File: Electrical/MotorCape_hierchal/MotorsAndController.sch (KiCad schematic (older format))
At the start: 5 parts, among them J1 Motor1, J2 DualMotorController_PWR, J4 DualMotorController_SIG, J5 Motor2

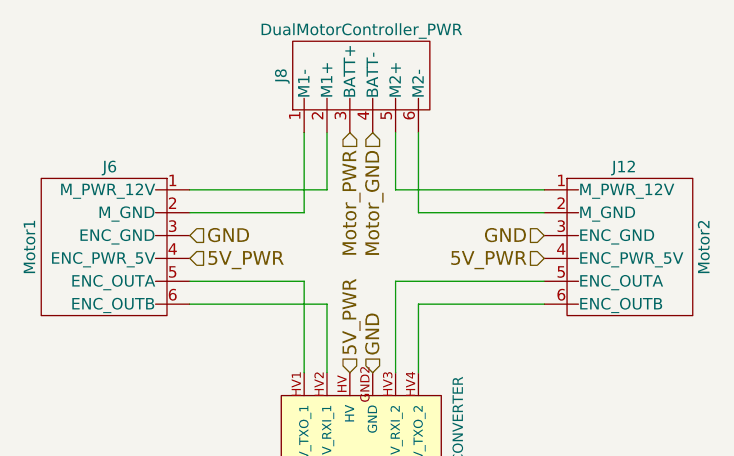
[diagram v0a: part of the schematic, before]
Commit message: trying to lay-out things. lots of via's, this could be a bit messy
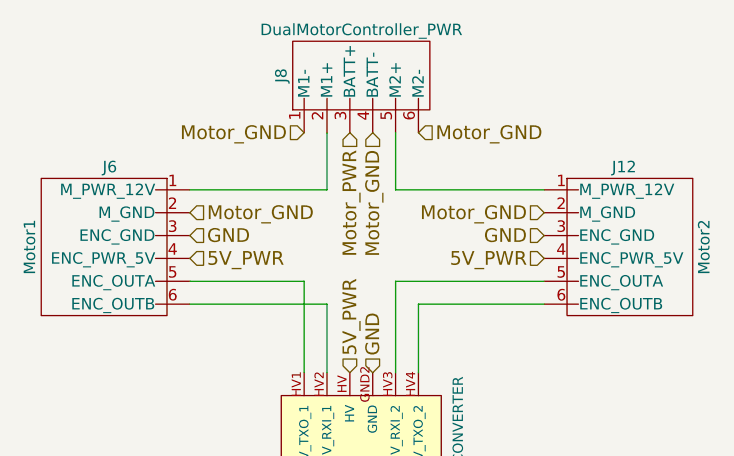
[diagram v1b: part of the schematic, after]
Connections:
- net Motor_GND: now also J1.2 (M_GND), J2.1 (M1-), J2.6 (M2-), J5.2 (M_GND)
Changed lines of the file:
@@
 $Descr A4 11693 8268
 encoding utf-8
-Sheet 3 4
+Sheet 2 4
 Title ""
 Date ""
@@
 $EndComp
 Wire Wire Line
-	3300 1700 3300 1950
-Wire Wire Line
-	3300 1950 2700 1950
-Wire Wire Line
-	3200 1700 3200 2050
-Wire Wire Line
-	3200 2050 2700 2050
-Wire Wire Line
-	3700 1700 3700 2050
-Wire Wire Line
-	3700 2050 4250 2050
-Wire Wire Line
 	3600 1700 3600 1950
 Wire Wire Line
@@
 	0    -1   -1   0
 $EndComp
+Wire Wire Line
+	3300 1700 3300 1950
+Wire Wire Line
+	3300 1950 2700 1950
+Text HLabel 2700 2050 2    60   Input ~ 0
+Motor_GND
+Text HLabel 3200 1700 0    60   Input ~ 0
+Motor_GND
+Text HLabel 3700 1700 2    60   Input ~ 0
+Motor_GND
+Text HLabel 4250 2050 0    60   Input ~ 0
+Motor_GND
 $EndSCHEMATC

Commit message: pushing changes while routing. still not done yet
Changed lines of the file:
@@
 AR Path="/5ACB9F03/5AC8852E" Ref="J10"  Part="1"
 AR Path="/5ACC6682/5AC8852E" Ref="J16"  Part="1"
-F 0 "J10" H 3500 5700 50  0000 C CNN
+F 0 "J4" H 3500 5700 50  0000 C CNN
 F 1 "DualMotorController_SIG" V 3300 5400 50  0000 C CNN
 F 2 "MotorCapeComponents:Pin_Header_Latched_1x05" H 3150 5350 50  0001 C CNN
@@
 AR Path="/5ACB9F03/5AC89C0C" Ref="J8"  Part="1"
 AR Path="/5ACC6682/5AC89C0C" Ref="J14"  Part="1"
-F 0 "J8" H 3450 1800 50  0000 C CNN
+F 0 "J2" H 3450 1800 50  0000 C CNN
 F 1 "DualMotorController_PWR" V 3650 1450 50  0000 C CNN
 F 2 "Connectors_Phoenix:PhoenixContact_MSTBA-G_06x5.08mm_Angled" H 3350 1450 50  0001 C CNN
@@
 AR Path="/5ACB9F03/5AC89F1B" Ref="J6"  Part="1"
 AR Path="/5ACC6682/5AC89F1B" Ref="J13"  Part="1"
-F 0 "J6" H 2350 2550 50  0000 C CNN
+F 0 "J1" H 2350 2550 50  0000 C CNN
 F 1 "Motor1" V 2700 2200 50  0000 C CNN
 F 2 "MotorCapeComponents:Pin_Header_Latched_1x06" H 2150 2200 50  0001 C CNN
@@
 AR Path="/5ACB9F03/5AC89F69" Ref="J12"  Part="1"
 AR Path="/5ACC6682/5AC89F69" Ref="J17"  Part="1"
-F 0 "J12" H 4600 2550 50  0000 C CNN
+F 0 "J5" H 4600 2550 50  0000 C CNN
 F 1 "Motor2" V 4950 2200 50  0000 C CNN
 F 2 "MotorCapeComponents:Pin_Header_Latched_1x06" H 4400 2200 50  0001 C CNN
@@
 AR Path="/5ACC6682/5AC8C87A" Ref="B3"  Part="1"
 AR Path="/5ACB9F03/5AC8C87A" Ref="B2"  Part="1"
-F 0 "B2" H 2950 3850 45  0000 L BNN
+F 0 "B1" H 2950 3850 45  0000 L BNN
 F 1 "SPARKFUN_LOGIC_LEVEL_CONVERTER" H 2950 3000 45  0000 L BNN
 F 2 "Sparkfun_Boards:SPARKFUN_LOGIC_LEVEL_CONVERTER" H 3500 3850 20  0001 C CNN

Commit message: pushing latest motor controller layout changes
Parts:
- renumbered J5 to BL1, J1 to FL1, J2 to Left_PWR1, J4 to Left_SIG1, B1 to Left_Shifters1
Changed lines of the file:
@@
 $Descr A4 11693 8268
 encoding utf-8
-Sheet 2 4
+Sheet 3 4
 Title ""
 Date ""
@@
 $EndDescr
 $Comp
-L DualMotorController_Signal J4
+L DualMotorController_Signal Left_SIG1
 U 1 1 5AC8852E
 P 3500 5350
-AR Path="/5AC8802A/5AC8852E" Ref="J4"  Part="1"
+AR Path="/5AC8802A/5AC8852E" Ref="Left_SIG1"  Part="1"
 AR Path="/5ACA5F87/5AC8852E" Ref="J?"  Part="1"
-AR Path="/5ACB9F03/5AC8852E" Ref="J10"  Part="1"
-AR Path="/5ACC6682/5AC8852E" Ref="J16"  Part="1"
-F 0 "J4" H 3500 5700 50  0000 C CNN
+AR Path="/5ACB9F03/5AC8852E" Ref="Top_SIG1"  Part="1"
+AR Path="/5ACC6682/5AC8852E" Ref="Right_SIG1"  Part="1"
+F 0 "Right_SIG1" H 3500 5700 50  0000 C CNN
 F 1 "DualMotorController_SIG" V 3300 5400 50  0000 C CNN
 F 2 "MotorCapeComponents:Pin_Header_Latched_1x05" H 3150 5350 50  0001 C CNN
@@
 M2_DIR
 $Comp
-L DualMotorController_Power J2
+L DualMotorController_Power Left_PWR1
 U 1 1 5AC89C0C
 P 3450 1450
-AR Path="/5AC8802A/5AC89C0C" Ref="J2"  Part="1"
+AR Path="/5AC8802A/5AC89C0C" Ref="Left_PWR1"  Part="1"
 AR Path="/5ACA5F87/5AC89C0C" Ref="J?"  Part="1"
-AR Path="/5ACB9F03/5AC89C0C" Ref="J8"  Part="1"
-AR Path="/5ACC6682/5AC89C0C" Ref="J14"  Part="1"
-F 0 "J2" H 3450 1800 50  0000 C CNN
+AR Path="/5ACB9F03/5AC89C0C" Ref="Top_PWR1"  Part="1"
+AR Path="/5ACC6682/5AC89C0C" Ref="Right_PWR1"  Part="1"
+F 0 "Right_PWR1" H 3450 1800 50  0000 C CNN
 F 1 "DualMotorController_PWR" V 3650 1450 50  0000 C CNN
 F 2 "Connectors_Phoenix:PhoenixContact_MSTBA-G_06x5.08mm_Angled" H 3350 1450 50  0001 C CNN
@@
 $EndComp
 $Comp
-L MotorConnector J1
+L MotorConnector FL1
 U 1 1 5AC89F1B
 P 2350 2200
-AR Path="/5AC8802A/5AC89F1B" Ref="J1"  Part="1"
+AR Path="/5AC8802A/5AC89F1B" Ref="FL1"  Part="1"
 AR Path="/5ACA5F87/5AC89F1B" Ref="J?"  Part="1"
-AR Path="/5ACB9F03/5AC89F1B" Ref="J6"  Part="1"
-AR Path="/5ACC6682/5AC89F1B" Ref="J13"  Part="1"
-F 0 "J1" H 2350 2550 50  0000 C CNN
+AR Path="/5ACB9F03/5AC89F1B" Ref="FlagWheel1"  Part="1"
+AR Path="/5ACC6682/5AC89F1B" Ref="FR1"  Part="1"
+F 0 "FR1" H 2350 2550 50  0000 C CNN
 F 1 "Motor1" V 2700 2200 50  0000 C CNN
 F 2 "MotorCapeComponents:Pin_Header_Latched_1x06" H 2150 2200 50  0001 C CNN
@@
 $EndComp
 $Comp
-L MotorConnector J5
+L MotorConnector BL1
 U 1 1 5AC89F69
 P 4600 2200
-AR Path="/5AC8802A/5AC89F69" Ref="J5"  Part="1"
+AR Path="/5AC8802A/5AC89F69" Ref="BL1"  Part="1"
 AR Path="/5ACA5F87/5AC89F69" Ref="J?"  Part="1"
-AR Path="/5ACB9F03/5AC89F69" Ref="J12"  Part="1"
-AR Path="/5ACC6682/5AC89F69" Ref="J17"  Part="1"
-F 0 "J5" H 4600 2550 50  0000 C CNN
+AR Path="/5ACB9F03/5AC89F69" Ref="DrawBridge1"  Part="1"
+AR Path="/5ACC6682/5AC89F69" Ref="BR1"  Part="1"
+F 0 "BR1" H 4600 2550 50  0000 C CNN
 F 1 "Motor2" V 4950 2200 50  0000 C CNN
 F 2 "MotorCapeComponents:Pin_Header_Latched_1x06" H 4400 2200 50  0001 C CNN
@@
 P 3500 3400
 AR Path="/5AC8C87A" Ref="B?"  Part="1"
-AR Path="/5AC8802A/5AC8C87A" Ref="B1"  Part="1"
-AR Path="/5ACC6682/5AC8C87A" Ref="B3"  Part="1"
-AR Path="/5ACB9F03/5AC8C87A" Ref="B2"  Part="1"
-F 0 "B1" H 2950 3850 45  0000 L BNN
+AR Path="/5AC8802A/5AC8C87A" Ref="Left_Shifters1"  Part="1"
+AR Path="/5ACC6682/5AC8C87A" Ref="Right_Shifters1"  Part="1"
+AR Path="/5ACB9F03/5AC8C87A" Ref="Top_Shifters1"  Part="1"
+F 0 "Right_Shifters1" H 2950 3850 45  0000 L BNN
 F 1 "SPARKFUN_LOGIC_LEVEL_CONVERTER" H 2950 3000 45  0000 L BNN
 F 2 "Sparkfun_Boards:SPARKFUN_LOGIC_LEVEL_CONVERTER" H 3500 3850 20  0001 C CNN
